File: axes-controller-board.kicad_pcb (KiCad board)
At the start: 4 copper layers, 203.1 x 102.9 mm, 161 parts, among them IC1 TPS5450QDDARQ1, IC2 ACS37800KMACTR-030B3-SPI, IC3 ACS37800KMACTR-030B3-SPI, IC4 ACS37800KMACTR-030B3-SPI, IC5 STM32H723ZGT6, J1 Conn_ST_STDC14, J10 Conn_01x08, J11 Conn_01x04, J12 Conn_01x08, J13 Conn_01x04, J14 Conn_01x08, J15 Conn_01x08, J16 Conn_01x04, J17 Conn_01x08, J18 Conn_01x08, J19 Conn_01x04, J2 Conn_01x03, J20 Conn_01x08, J21 Conn_01x08, J22 Conn_01x04, J23 Conn_01x08, J24 Conn_01x08, J25 Conn_01x04, J26 Conn_01x08, J27 Raspberry_Pi_2_3, J28 DC1, J29 DC2, J3 Conn_01x03, J30 DC3, J31 Conn_01x08, J32 Conn_01x08, J33 DC1, J34 Conn_01x08, J35 Conn_01x08, J36 Conn_01x08, J37 ENDSTOP, J38 ENDSTOP, J39 ENDSTOP, J4 Conn_01x03, J40 Conn_01x03, J5 DRIVER, J6 NTC, J7 DRIVER, J8 NTC, J9 Conn_01x08, SW1 RESET, U1 LM1117MP-3.3, U3 UA9637A, U5 UA9637A, U7 UA9637A, Y1 16MHz

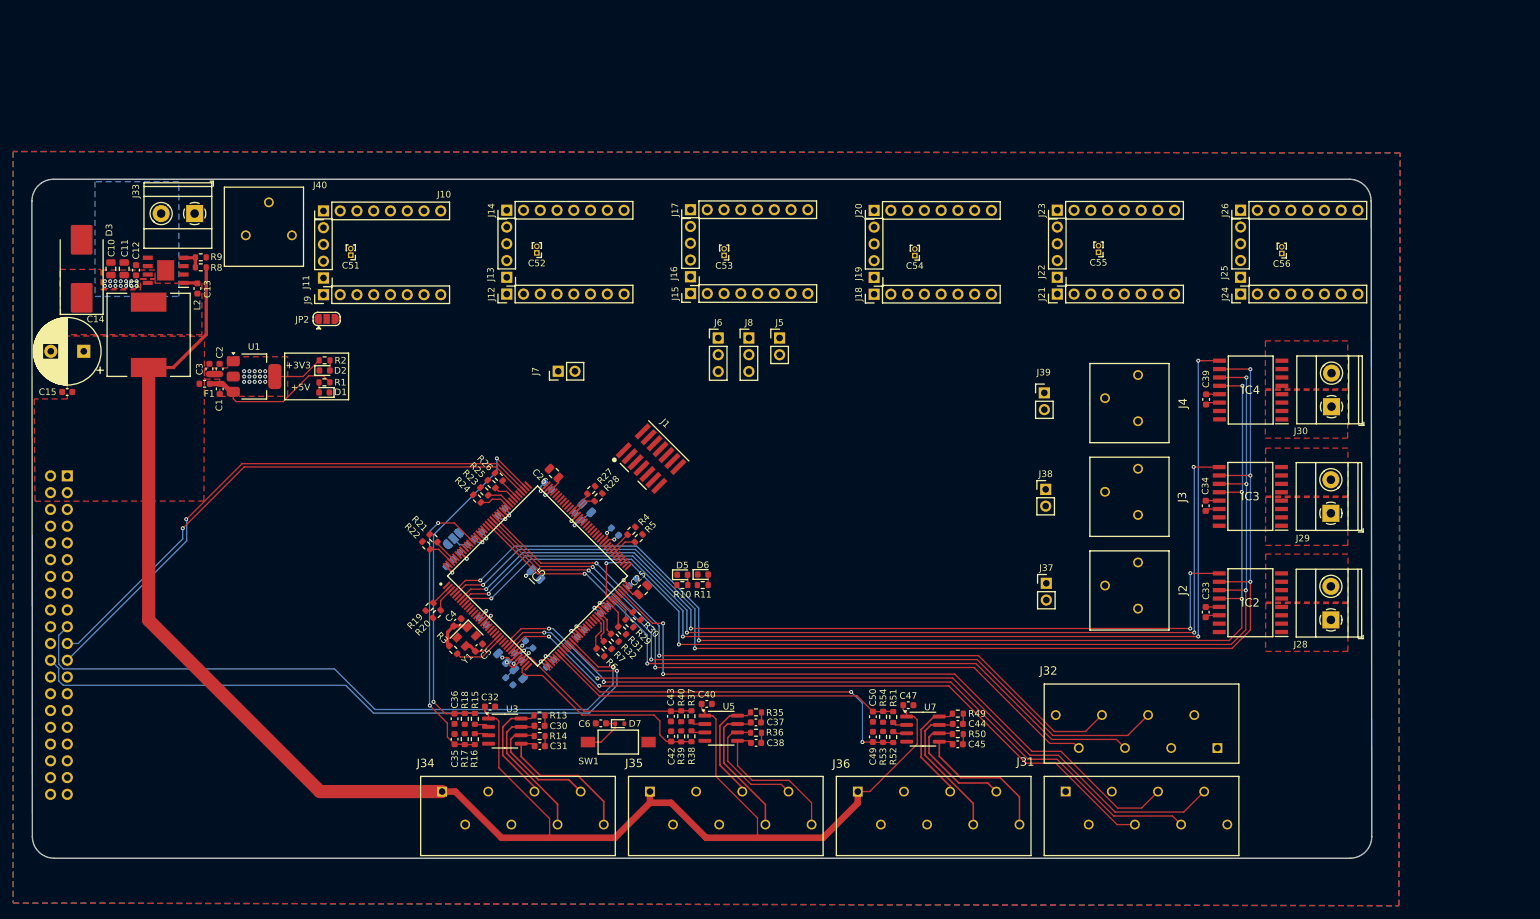
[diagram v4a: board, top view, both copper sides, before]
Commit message: feat: stepper motors connections to micro
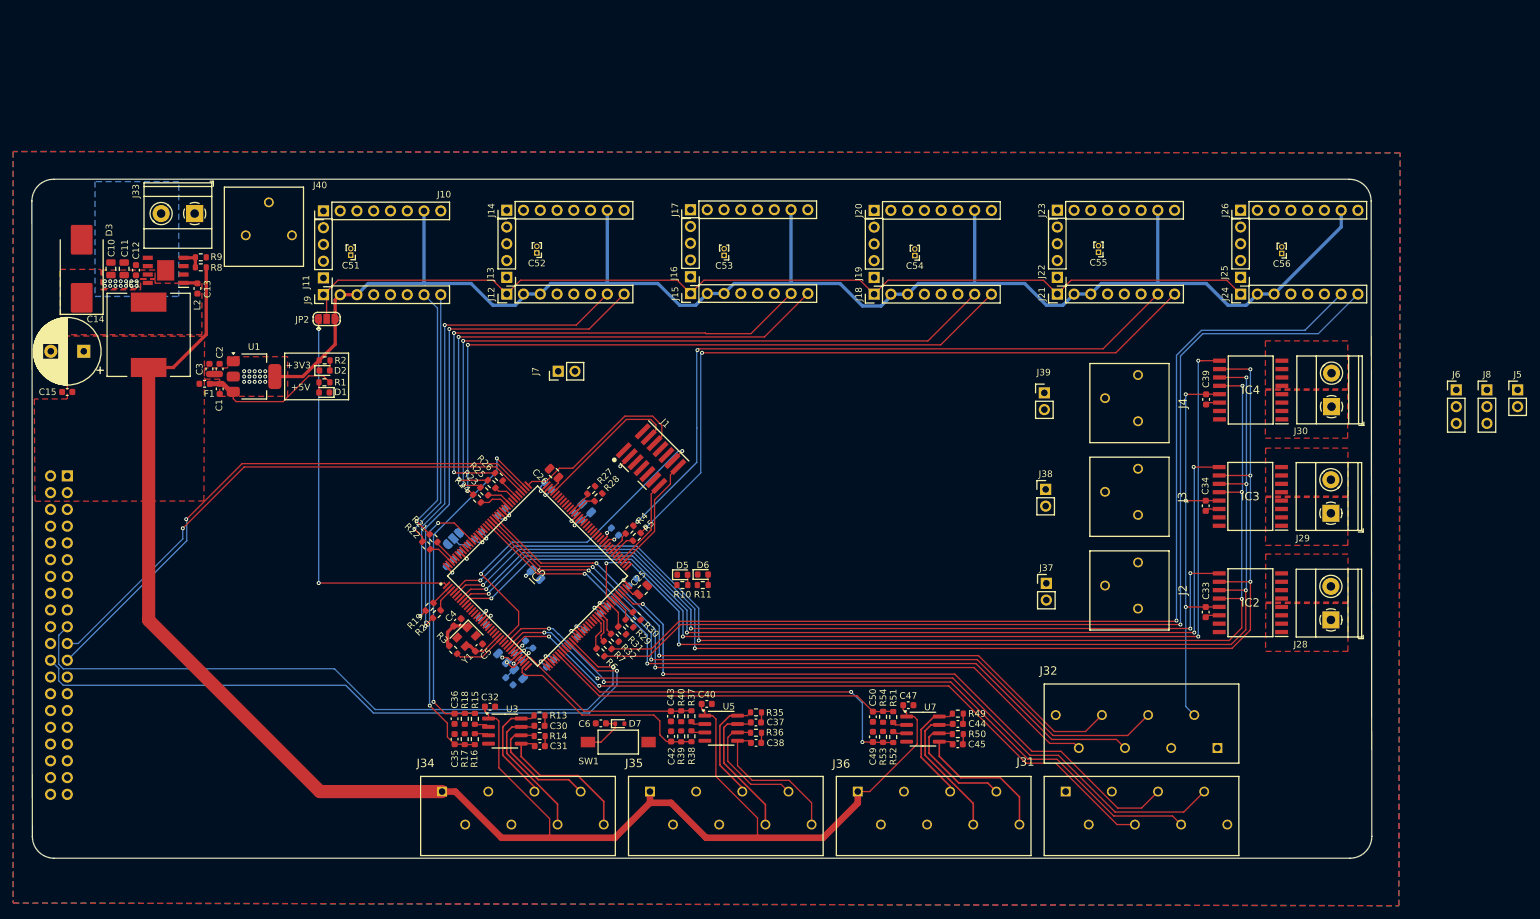
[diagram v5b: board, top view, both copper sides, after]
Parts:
- moved J8 112.1 mm to (280.4, 74.0)
- moved J5 112.1 mm to (285.0, 74.0)
- moved J6 112.1 mm to (275.7, 74.0)
- moved R5 0.36 mm to (151.5, 96.3)
- moved R4 0.35 mm to (150.4, 95.2)
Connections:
- J15 pad 8: /DIR_P2 -> /DIR_P1
- R25 pad 1: /DIR_P2 -> /DIR_P1
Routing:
- net +3V3: track 60.6 -> 360.6 mm, vias 31 -> 35
- net /DIR_F: track 0.00 -> 160.8 mm, vias 0 -> 1
- net /STEP_F: track 0.00 -> 156.4 mm, vias 0 -> 1
- net /EN_MOD: track 0.00 -> 151.6 mm
- net /DIR_YAW: track 0.00 -> 106.5 mm, vias 0 -> 2
- net /DIR_P2: track 0.00 -> 105.8 mm, vias 0 -> 2
- net /STEP_P2: track 0.00 -> 105.1 mm, vias 0 -> 2
- net /STEP_YAW: track 0.00 -> 103.9 mm, vias 0 -> 2
- net /DIR_P1: track 0.00 -> 81.7 mm, vias 0 -> 2
- net /STEP_P1: track 0.00 -> 81.0 mm, vias 0 -> 2
- net /DIR_Z2: track 0.00 -> 76.8 mm, vias 0 -> 2
- net /STEP_Z2: track 0.00 -> 73.4 mm, vias 0 -> 2
- net /MCU/EN_STEPPERS: track 0.00 -> 59.6 mm, vias 0 -> 2
- net /MCU/~{RST}: track 7.07 -> 61.0 mm, vias 0 -> 2
- net /DIR_Z1: track 0.00 -> 39.6 mm, vias 0 -> 1
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
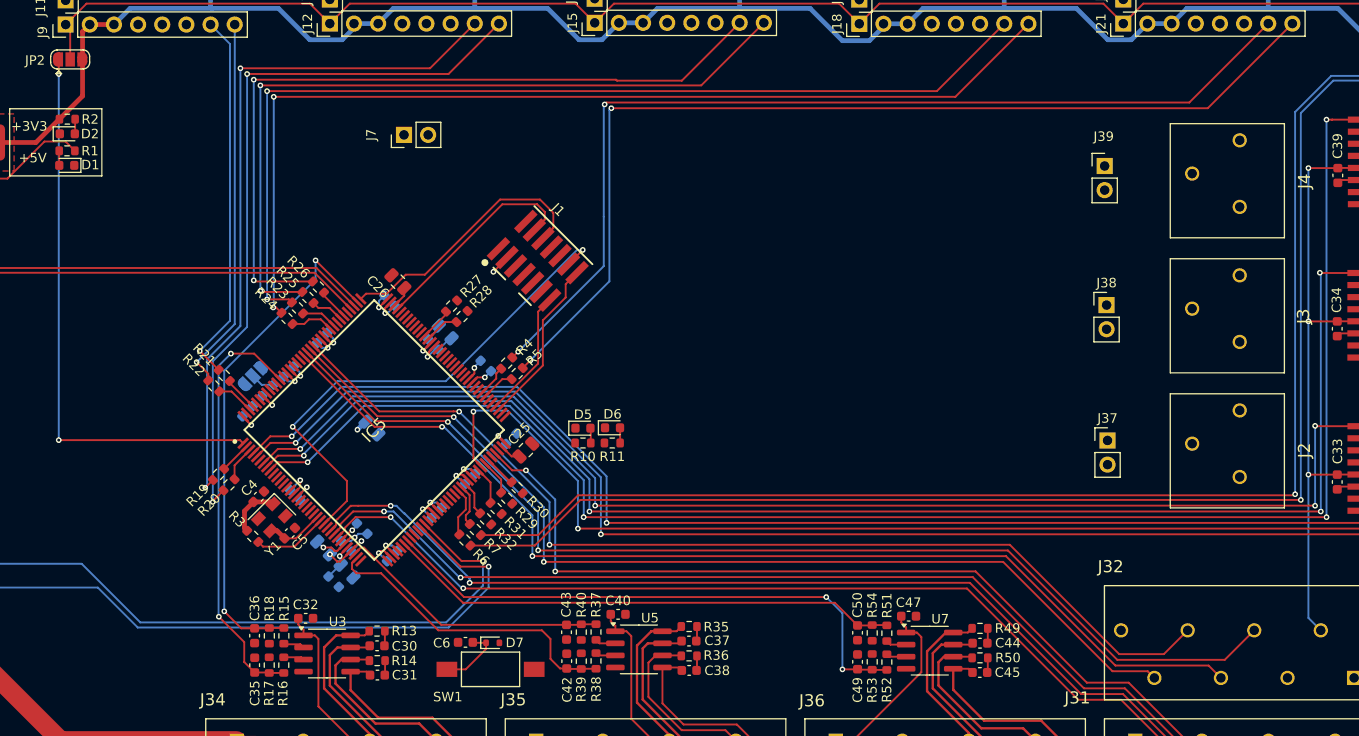
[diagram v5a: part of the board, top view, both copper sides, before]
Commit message: feat: dc driver connections
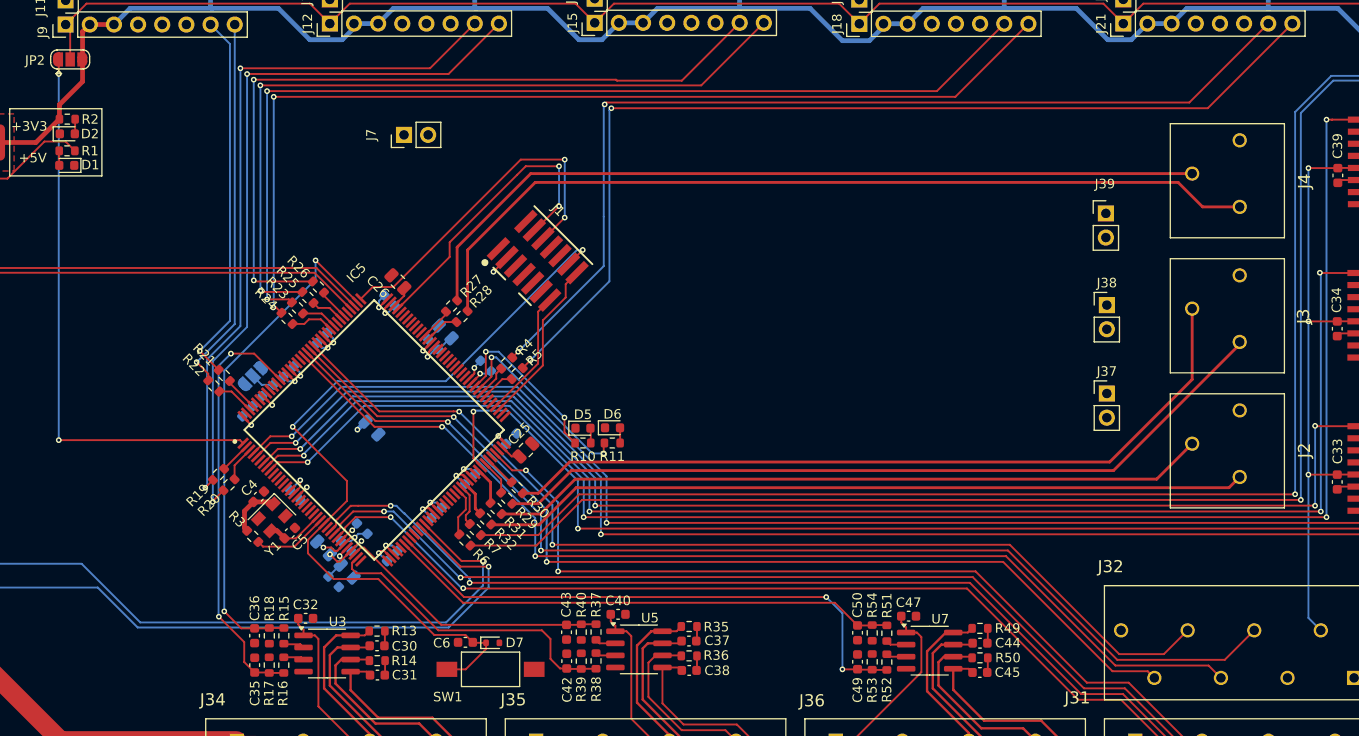
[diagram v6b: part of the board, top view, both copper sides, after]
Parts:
- moved J39 4.99 mm to (213.4, 79.5)
- moved J37 4.93 mm to (213.5, 98.4)
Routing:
- net /MCU/Y2_DC_PWM_1: track 0.00 -> 91.6 mm
- net /MCU/Y2_DC_PWM_2: track 0.00 -> 86.1 mm
- net /MCU/Y1_DC_PWM_1: track 0.00 -> 83.7 mm
- net /MCU/Y1_DC_PWM_2: track 0.00 -> 82.8 mm
- net /MCU/X_DC_PWM_1: track 0.00 -> 80.9 mm
- net /MCU/X_DC_PWM_2: track 0.00 -> 75.7 mm
- net /MCU/~{RST}: track 61.0 -> 86.0 mm
- net /MCU/LED_2: track 0.00 -> 21.1 mm, vias 0 -> 2
- net /MCU/LED_1: track 0.00 -> 18.4 mm, vias 0 -> 2
- net /MCU/SWDIO: track 22.7 -> 31.9 mm, vias 0 -> 2
- net /MCU/SWCLK: track 28.3 -> 36.8 mm, vias 0 -> 2
